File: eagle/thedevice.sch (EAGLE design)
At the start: 53 parts, among them J1 SBH11-PBPC-D10, J2 SBH11-PBPC-D12, U1 ADXL345, U2 BMP180, U3 HTU21DSMD, U4 LSM9DS0, U5 SPI_FLASH-X25XXSMD, U6 LTC3426, U7 LTC3426, X1 molex

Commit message: made all changes for V1.1
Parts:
- removed C11, C13: 10uF, SparkFun-Capacitors:CAP0603-CAP
- removed C12, C14: 100nF, SparkFun-Capacitors:CAP0603-CAP
- removed JP2: (no value), SparkFun-Connectors:M04PTH
- removed U1: ADXL345, SparkFun:ADXL345
- removed U5: SPI_FLASH-X25XXSMD, SparkFun-DigitalIC:SPI_FLASH-X25XXSMD
- added JP3: M02PTH, SparkFun-Connectors:M02PTH
- added R15: (no value), SparkFun-Passives:RESISTOR0603-RES
- added S3: (no value), SparkFun-Electromechanical:SWITCH-SPDTSMD2
- added U$17: SPI_FLASH-X25XXSMD1, SparkFun-DigitalIC:SPI_FLASH-X25XXSMD1
- added U$28: M08X2, SparkFun-Connectors:M08X2
- JP1: value 2X6 FEMALE -> (none); device SparkFun-Connectors:M06X2PTH_FEMALE -> SparkFun-Connectors:M05NO_SILK; PARTNO PPTC062LJBN-RC -> (none)
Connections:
- removed net ADXLINT1: J2.5, U1.INT1
- removed net ADXLINT2: J2.3, U1.INT2
- removed net N$13: C14.2, U1.VS
- new net N$11: D4.C, S3.P
- new net N$12: D4.A, JP3.2, R15.2
- new net N$15: U$28.4
- new net N$16: U$28.2
- new net UA10: J1.12, U$28.3
- new net UA8: J2.3, U$28.8
- new net UA9: J2.5, U$28.9
- net 3V3: now also J1.2, J2.2, J2.23, JP1.5, R6.2, U$17.HOLD, U$17.VCC, U$17.WP, U$28.15; no longer C12.2, JP1.3, JP2.1, U1.CS, U1.VDD, U5.HOLD, U5.VCC, U5.WP
- net 5V0: now also U$28.16; no longer JP1.1
- net ENABLE3V: no longer J1.12
- net FLASHCS: now also U$17.CS; no longer U5.CS
- net GND: now also U$17.GND, U$28.6; no longer C11.1, C12.1, C13.1, C14.1, JP2.2, U1.GND, U1.GND1, U1.GND2, U1.SDO, U5.GND
- net N$3: now also JP3.1, R15.1; no longer D4.A
- net P4MISO: now also U$17.MISO; no longer U5.MISO
- net P4MOSI: now also U$17.MOSI; no longer U5.MOSI
- net P4SPICLK: now also U$17.SCK; no longer U5.SCK
- net SCL: now also JP1.2; no longer JP2.4, U1.SCL
- net SDA: now also JP1.1; no longer JP2.3, U1.SDA
- net UA0: now also U$28.5; no longer JP1.5
- net UA1: now also U$28.7; no longer JP1.7
- net UA2: now also U$28.1; no longer JP1.9
- net UA3: now also U$28.11; no longer JP1.11
- net UA4: now also U$28.13; no longer JP1.12
- net UA5: now also U$28.14; no longer JP1.10
- net UA6: now also U$28.12; no longer JP1.8
- net UA7: now also U$28.10; no longer JP1.6
- net VIN: now also S3.O; no longer D4.C, J1.2, J2.2, J2.23, JP1.2, R6.2
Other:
- note removed: "VDDR"
- moved on the sheet: BAT1

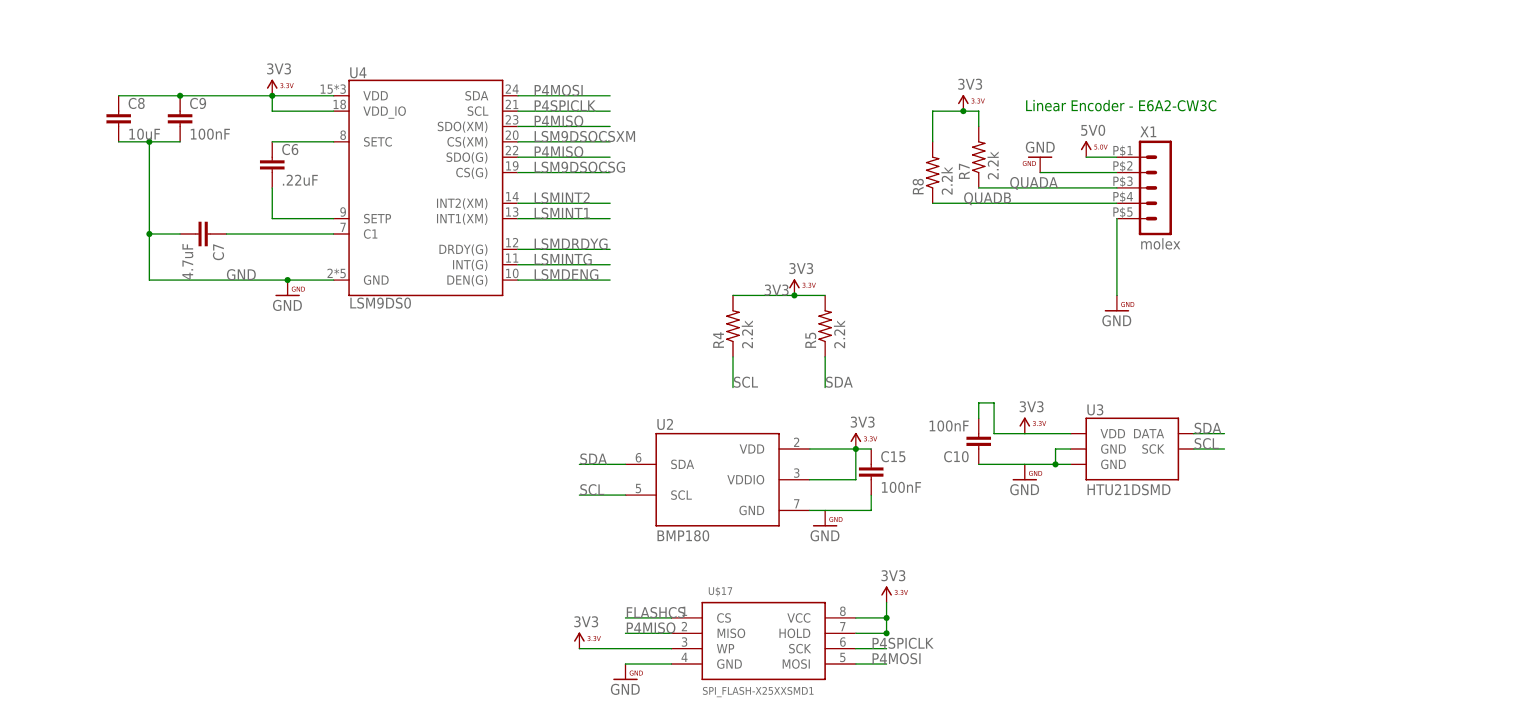
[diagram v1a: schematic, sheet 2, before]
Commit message: Made all V1.2 changes except newtons laws
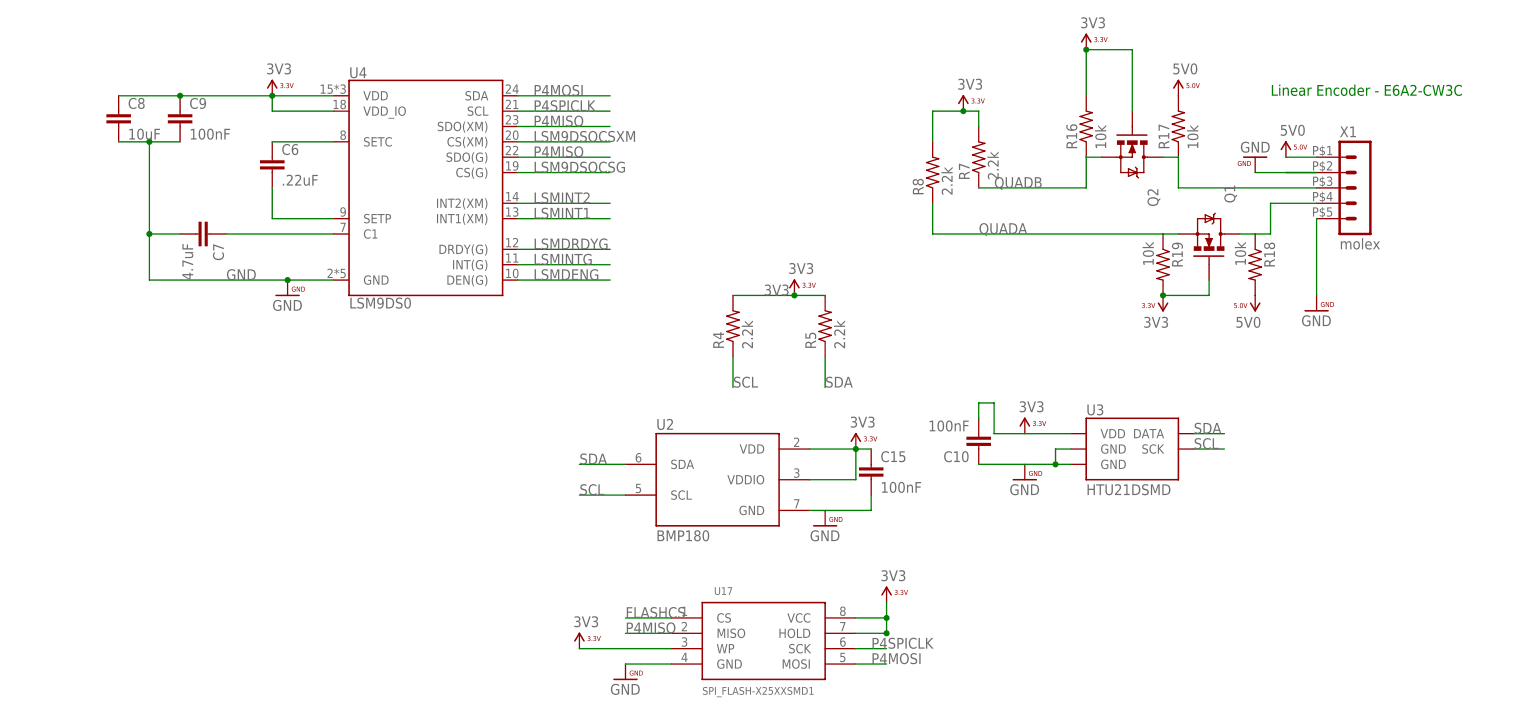
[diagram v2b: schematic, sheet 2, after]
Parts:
- added Q1, Q2: MOSFET-NCHANNEL2N7002PW, SparkFun-DiscreteSemi:MOSFET-NCHANNEL2N7002PW
- added R16, R17, R18, R19: 10k, SparkFun-Resistors:RESISTOR0603
- renumbered JPROG to JP, U$17 to U17, U$28 to J28
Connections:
- removed net N$15: J28.4
- removed net N$16: J28.2
- removed net UA5: J2.10, J28.14
- new net N$14: Q2.D, R17.1, X1.3
- new net N$19: Q1.D, R18.1, X1.4
- net 3V3: now also Q1.G, Q2.G, R16.2, R19.2
- net 5V0: now also R17.2, R18.2
- net GND: now also J28.14, J28.2, J28.4
- net LSMINT1: now also J2.10; no longer J2.13
- net QUADA: now also Q1.S, R19.1, R8.1; no longer R7.1, X1.3
- net QUADB: now also Q2.S, R16.1, R7.1; no longer R8.1, X1.4
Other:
- moved on the sheet: X1
